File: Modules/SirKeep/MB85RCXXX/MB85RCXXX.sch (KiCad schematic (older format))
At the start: 15 parts, among them J1 Conn_01x05, U1 MB85RC256V

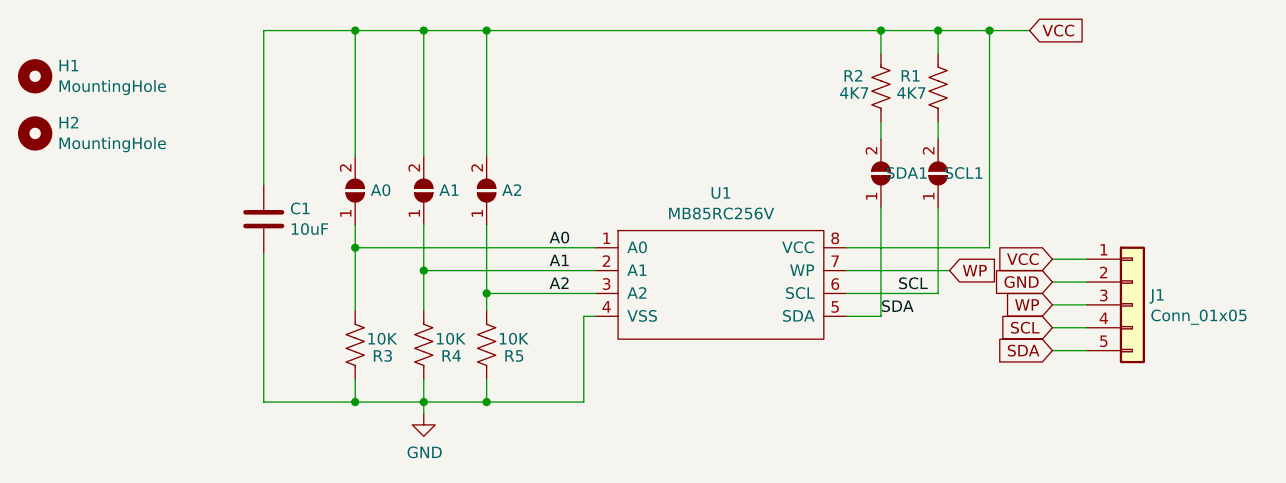
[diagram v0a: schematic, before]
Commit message: MB85RXXX Added in place of MB85RC256V
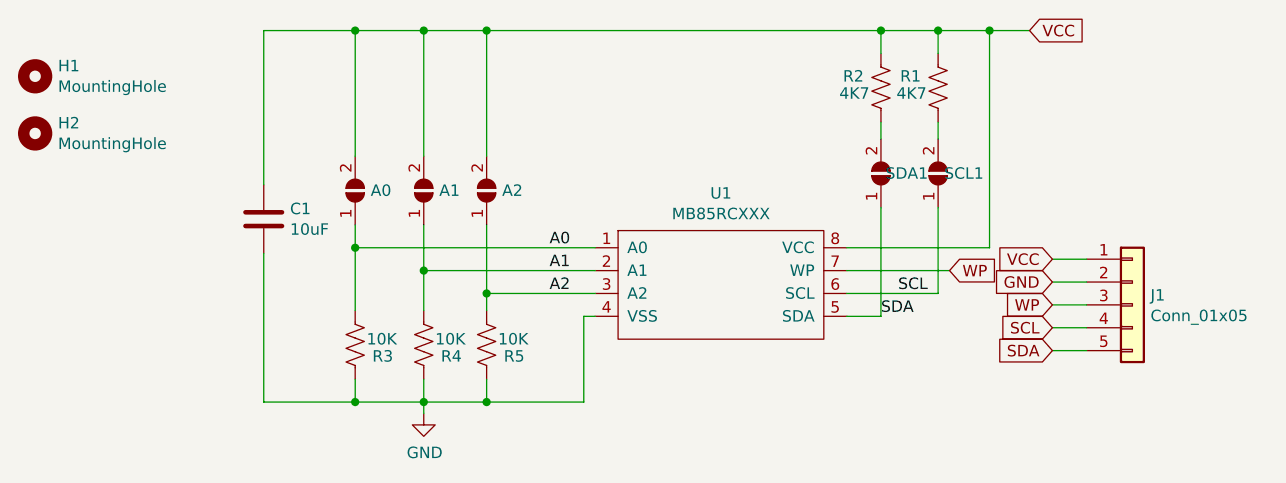
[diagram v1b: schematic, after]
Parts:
- U1: value MB85RC256V -> MB85RCXXX
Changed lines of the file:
@@
 encoding utf-8
 Sheet 1 1
-Title "MB85RC256V Based FRAM Module"
+Title "MB85RCXXX Based FRAM Module"
 Date "2019-12-06"
 Rev "1"
@@
 Comment1 "SirBoard"
 Comment2 "SirKeep"
-Comment3 "MB85RC256V"
+Comment3 "MB85RC64, MB85RC128, MB85RC256, MB85RC512, MB85RC1M"
 Comment4 ""
 $EndDescr
@@
 P 4450 2300
 F 0 "U1" H 4450 2738 50  0000 C CNN
-F 1 "MB85RC256V" H 4450 2648 50  0000 C CNN
+F 1 "MB85RCXXX" H 4450 2648 50  0000 C CNN
 F 2 "Package_SO:SO-8_3.9x4.9mm_P1.27mm" H 4450 2300 50  0001 C CNN
 F 3 "" H 4450 2300 50  0001 C CNN
